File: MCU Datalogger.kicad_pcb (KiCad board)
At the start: 2 copper layers, 58.5 x 39.9 mm, 29 parts, among them J1 Conn_01x04_Pin, J2 Conn_01x04_Pin, J3 Conn_01x09_Pin, J4 Conn_02x03_Odd_Even, U1 24LC1025, U2 24LC1025, U3 DS1337S_, U4 ATMEGA328P-AU, Y1 32.768KHz, Y2 16MHz

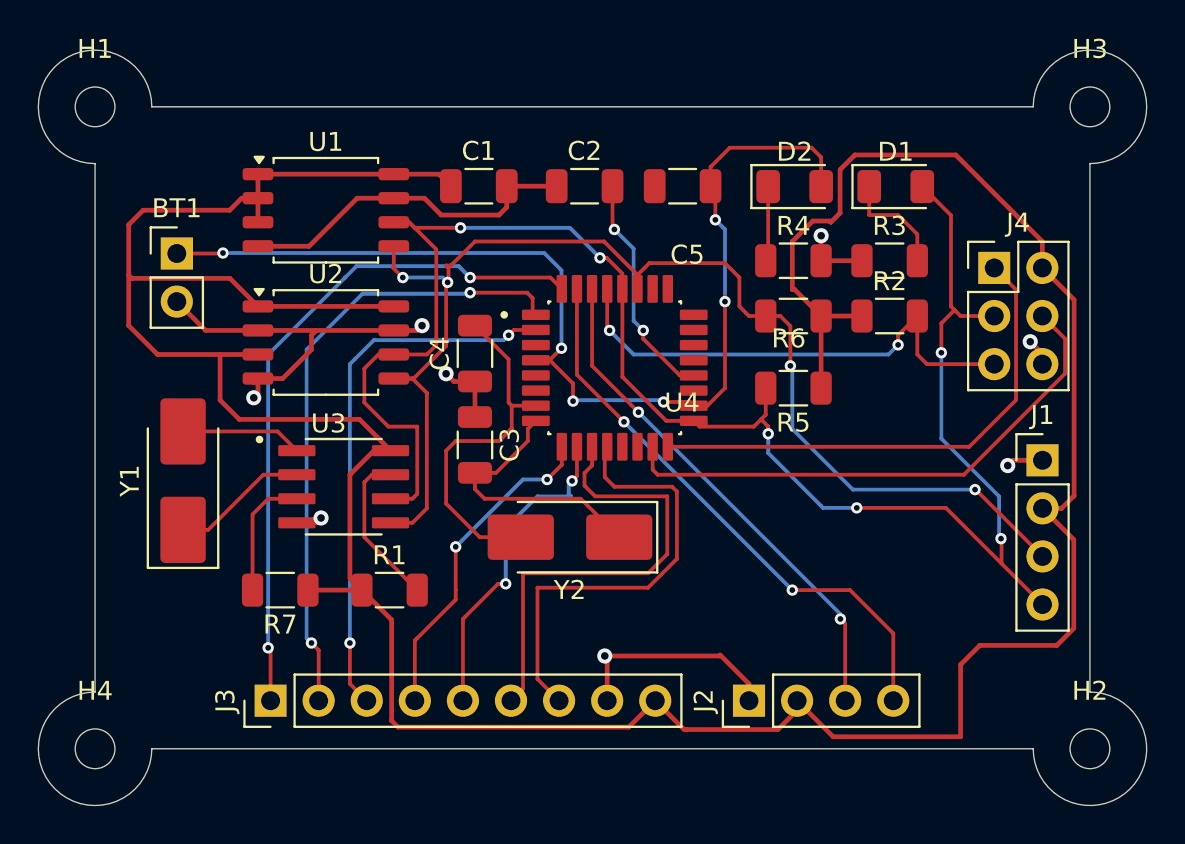
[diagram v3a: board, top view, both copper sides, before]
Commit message: routing done including copper fill
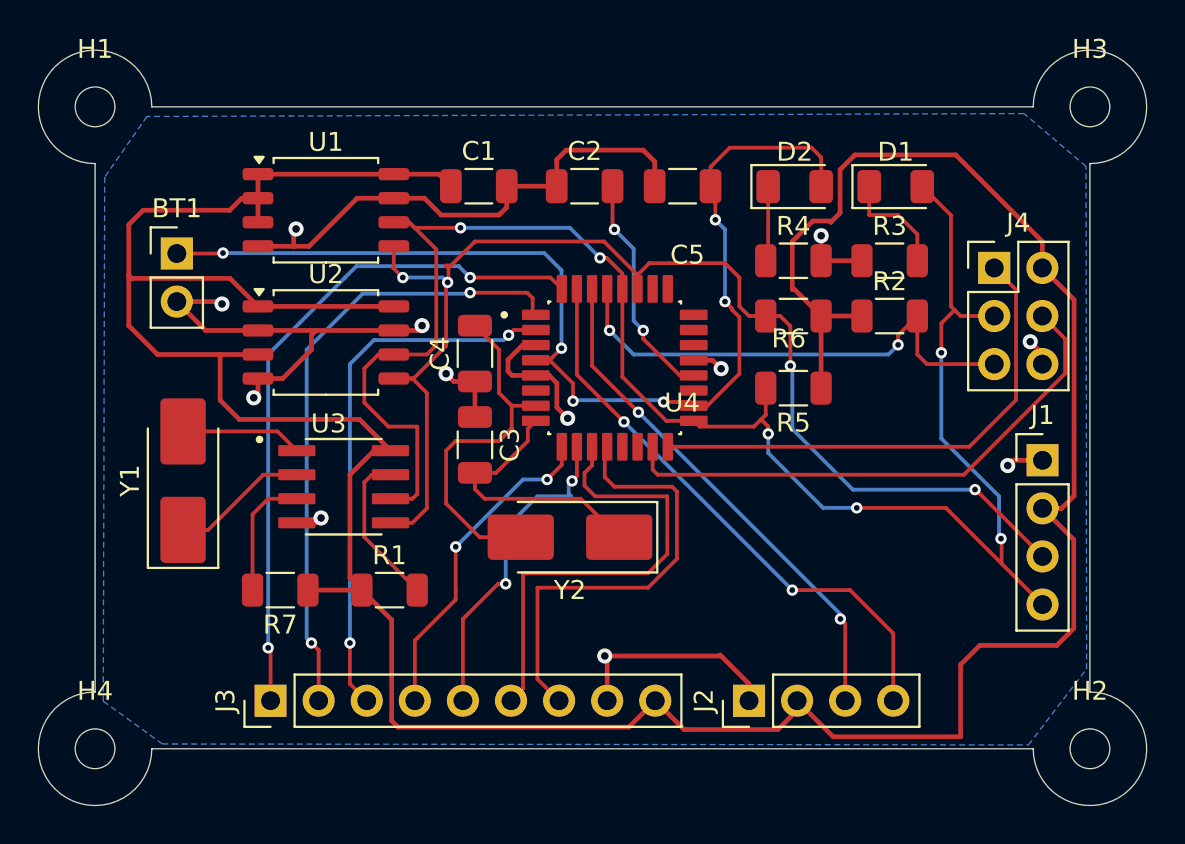
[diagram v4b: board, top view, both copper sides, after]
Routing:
- net GND: track 61.6 -> 82.3 mm, vias 8 -> 12
- added copper zone on B.Cu, net GND
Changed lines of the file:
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@@
+	)
+	(segment
+		(start 160.381 86.9071)
+		(end 160.381 86.848)
+		(width 0.2)
+		(layer "F.Cu")
+		(net 1)
+	)
+	(segment
+		(start 158.369 91.986)
+		(end 159.093 91.986)
+		(width 0.2)
+		(layer "F.Cu")
+		(net 1)
 	)
 	(segment
@@
 	)
 	(segment
-		(start 160.02 91.059)
-		(end 160.02 86.233)
+		(start 160.782 87.3081)
+		(end 160.381 86.9071)
+		(width 0.2)
+		(layer "F.Cu")
+		(net 1)
+	)
+	(segment
+		(start 159.093 91.986)
+		(end 160.782 90.297)
 		(width 0.2)
 		(layer "F.Cu")
@@
 	)
 	(segment
-		(start 159.093 91.986)
-		(end 160.02 91.059)
-		(width 0.2)
-		(layer "F.Cu")
-		(net 1)
-	)
-	(segment
 		(start 156.773965 91.790435)
 		(end 158.173435 91.790435)
@@
 	)
 	(segment
-		(start 160.02 86.233)
+		(start 160.381 86.848)
 		(end 160.02 86.487)
 		(width 0.2)
@@
 	)
 	(segment
+		(start 160.782 90.297)
+		(end 160.782 87.3081)
+		(width 0.2)
+		(layer "F.Cu")
+		(net 1)
+	)
+	(segment
 		(start 151.9936 90.8156)
 		(end 151.9936 91.7448)
@@
 	)
 	(segment
-		(start 158.369 91.986)
-		(end 159.093 91.986)
-		(width 0.2)
-		(layer "F.Cu")
-		(net 1)
-	)
-	(segment
 		(start 133.5024 83.9216)
 		(end 133.477 83.947)
@@
 	)
 	(segment
+		(start 151.13 80.391)
+		(end 151.13 78.994)
+		(width 0.25)
+		(layer "F.Cu")
+		(net 2)
+	)
+	(segment
+		(start 150.029 88.786)
+		(end 149.325622 88.786)
+		(width 0.25)
+		(layer "F.Cu")
+		(net 2)
+	)
+	(segment
+		(start 151.14 92.08132)
+		(end 151.710238 92.651558)
+		(width 0.25)
+		(layer "F.Cu")
+		(net 2)
+	)
+	(segment
+		(start 131.064 86.487)
+		(end 133.3246 86.487)
+		(width 0.25)
+		(layer "F.Cu")
+		(net 2)
+	)
+	(segment
 		(start 153.797 107.569)
 		(end 153.797 105.3338)
@@
 	)
 	(segment
+		(start 133.3246 86.487)
+		(end 133.4516 86.614)
+		(width 0.25)
+		(layer "F.Cu")
+		(net 2)
+	)
+	(segment
+		(start 151.13 78.994)
+		(end 151.638 78.486)
+		(width 0.25)
+		(layer "F.Cu")
+		(net 2)
+	)
+	(segment
 		(start 135.3505 91.3445)
 		(end 135.128 91.567)
@@
 	)
 	(segment
+		(start 150.029 90.386)
+		(end 150.732378 90.386)
+		(width 0.25)
+		(layer "F.Cu")
+		(net 2)
+	)
+	(segment
 		(start 159.7152 105.2068)
 		(end 159.766 105.156)
@@
 	)
 	(segment
+		(start 155.702 78.486)
+		(end 156.308 79.092)
+		(width 0.25)
+		(layer "F.Cu")
+		(net 2)
+	)
+	(segment
 		(start 132.588 88.011)
 		(end 135.3505 88.011)
@@
 	)
 	(segment
+		(start 159.3718 89.586)
+		(end 159.8168 90.031)
+		(width 0.25)
+		(layer "F.Cu")
+		(net 2)
+	)
+	(segment
+		(start 151.638 78.486)
+		(end 155.702 78.486)
+		(width 0.25)
+		(layer "F.Cu")
+		(net 2)
+	)
+	(segment
 		(start 136.652 90.551)
 		(end 138.176 89.027)
@@
 	)
 	(segment
+		(start 148.774 90.386)
+		(end 150.029 90.386)
+		(width 0.25)
+		(layer "F.Cu")
+		(net 2)
+	)
+	(segment
 		(start 143.764 88.011)
 		(end 144.018 87.757)
@@
 	)
 	(segment
+		(start 137.2362 82.7786)
+		(end 137.3632 82.6516)
+		(width 0.25)
+		(layer "F.Cu")
+		(net 2)
+	)
+	(segment
 		(start 159.766 105.156)
 		(end 161.29 106.68)
@@
 	)
 	(segment
+		(start 156.308 79.092)
+		(end 156.308 80.391)
+		(width 0.25)
+		(layer "F.Cu")
+		(net 2)
+	)
+	(segment
+		(start 137.2362 83.566)
+		(end 137.2362 82.7786)
+		(width 0.25)
+		(layer "F.Cu")
+		(net 2)
+	)
+	(segment
+		(start 135.3505 83.566)
+		(end 137.2362 83.566)
+		(width 0.25)
+		(layer "F.Cu")
+		(net 2)
+	)
+	(segment
 		(start 140.589 81.026)
 		(end 142.5255 81.026)
@@
 	)
 	(segment
+		(start 148.558 89.553622)
+		(end 148.558 90.17)
+		(width 0.25)
+		(layer "F.Cu")
+		(net 2)
+	)
+	(segment
 		(start 138.049 83.566)
 		(end 140.589 81.026)
@@
 	)
 	(segment
-		(start 135.3505 83.566)
+		(start 137.2362 83.566)
 		(end 138.049 83.566)
+		(width 0.25)
+		(layer "F.Cu")
+		(net 2)
+	)
+	(segment
+		(start 151.14 90.793622)
+		(end 151.14 92.08132)
 		(width 0.25)
 		(layer "F.Cu")
@@
 	)
 	(segment
+		(start 150.732378 90.386)
+		(end 151.14 90.793622)
+		(width 0.25)
+		(layer "F.Cu")
+		(net 2)
+	)
+	(segment
 		(start 135.3505 90.551)
 		(end 136.652 90.551)
@@
 	)
 	(segment
+		(start 149.325622 88.786)
+		(end 148.558 89.553622)
+		(width 0.25)
+		(layer "F.Cu")
+		(net 2)
+	)
+	(segment
 		(start 145.034 81.915)
 		(end 148.082 81.915)
@@
 	)
 	(segment
+		(start 148.558 90.17)
+		(end 148.774 90.386)
+		(width 0.25)
+		(layer "F.Cu")
+		(net 2)
+	)
+	(segment
 		(start 146.812 92.583)
 		(end 146.812 90.707)
@@
 		(start 165.098 83.0092)
 		(end 165.1 83.0072)
+		(width 0.25)
+		(layer "F.Cu")
+		(net 2)
+	)
+	(segment
+		(start 158.369 89.586)
+		(end 159.3718 89.586)
 		(width 0.25)
 		(layer "F.Cu")
@@
 	)
 	(via
+		(at 159.8168 90.031)
+		(size 0.8)
+		(drill 0.4)
+		(layers "F.Cu" "B.Cu")
+		(net 2)
+	)
+	(via
 		(at 165.1 83.0072)
 		(size 0.8)
@@
 	)
 	(via
+		(at 137.3632 82.6516)
+		(size 0.8)
+		(drill 0.4)
+		(layers "F.Cu" "B.Cu")
+		(net 2)
+	)
+	(via
+		(at 133.4516 86.614)
+		(size 0.8)
+		(drill 0.4)
+		(layers "F.Cu" "B.Cu")
+		(net 2)
+	)
+	(via
 		(at 135.128 91.567)
 		(size 0.8)
@@
 	)
 	(via
+		(at 151.710238 92.651558)
+		(size 0.8)
+		(drill 0.4)
+		(layers "F.Cu" "B.Cu")
+		(net 2)
+	)
+	(via
 		(at 145.288 90.297)
 		(size 0.8)
@@
 	)
 	(segment
+		(start 148.082 91.313)
+		(end 148.755 91.986)
+		(width 0.2)
+		(layer "F.Cu")
+		(net 6)
+	)
+	(segment
+		(start 148.082 89.027)
+		(end 148.082 91.313)
+		(width 0.2)
+		(layer "F.Cu")
+		(net 6)
+	)
+	(segment
 		(start 147.066 98.933)
 		(end 145.288 97.155)
@@
 	)
 	(segment
-		(start 146.812 87.757)
-		(end 148.59 89.535)
-		(width 0.2)
-		(layer "F.Cu")
-		(net 6)
-	)
-	(segment
 		(start 145.796 93.853)
 		(end 148.082 93.853)
@@
 	)
 	(segment
-		(start 148.59 89.535)
-		(end 148.59 91.821)
-		(width 0.2)
-		(layer "F.Cu")
-		(net 6)
-	)
-	(segment
-		(start 148.59 91.821)
-		(end 148.755 91.986)
+		(start 146.812 87.757)
+		(end 148.082 89.027)
 		(width 0.2)
 		(layer "F.Cu")
@@
 		(net 26)
 	)
+	(zone
+		(net 2)
+		(net_name "GND")
+		(layer "B.Cu")
+		(hatch edge 0.5)
+		(connect_pads
+			(clearance 0.5)
+		)
+		(min_thickness 0.25)
+		(filled_areas_thickness no)
+		(fill yes
+			(mode hatch)
+			(thermal_gap 0.5)
+			(thermal_bridge_width 0.5)
+			(hatch_thickness 1)
+			(hatch_gap 1.5)
+			(hatch_orientation 0)
+			(hatch_border_algorithm hatch_thickness)
+			(hatch_min_hole_area 0.3)
+		)
+		(polygon
+			(pts
+				(xy 175.8188 76.5556) (xy 129.4892 76.708) (xy 127.254 79.9084) (xy 127.1778 107.5944) (xy 130.302 109.855)
+				(xy 176.0474 109.9058) (xy 179.1208 105.8926) (xy 179.0954 79.3496)
+			)
+		)
+	)
 	(embedded_fonts no)

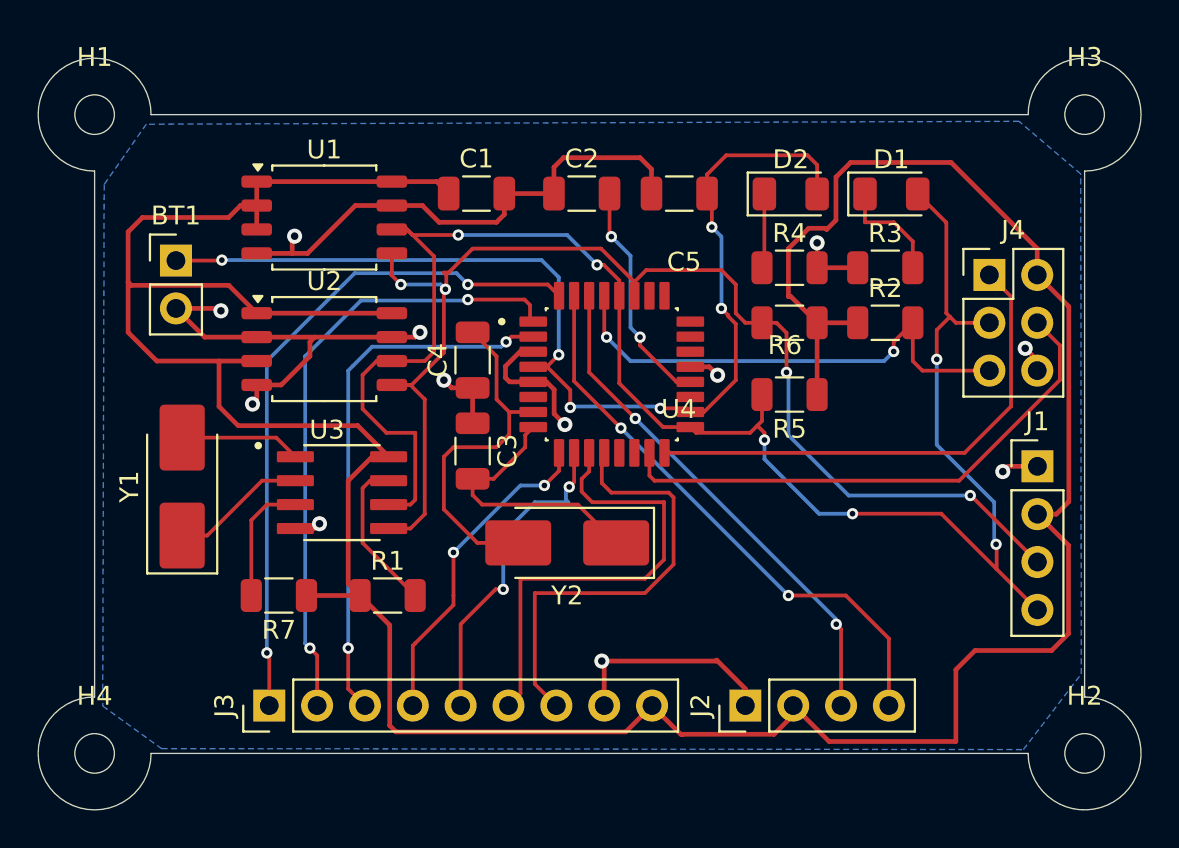
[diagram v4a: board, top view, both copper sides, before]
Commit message: silk screen labelling + routing + drc done
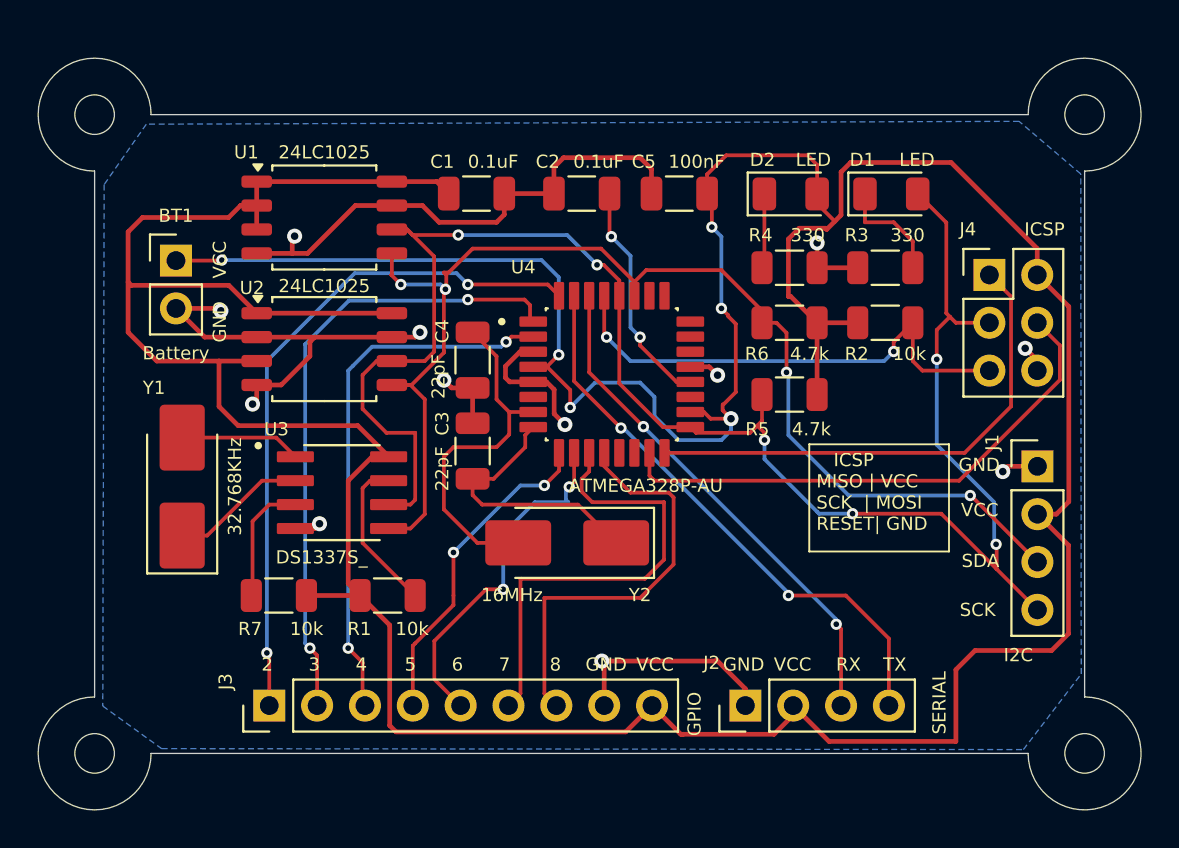
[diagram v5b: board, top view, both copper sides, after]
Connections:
- BT1 pad 1: Net-(BT1-+) -> /Vcc
- C5 pad 1: Net-(BT1-+) -> /Vcc
- D2 pad 2: Net-(BT1-+) -> /Vcc
- U4 pad 18: Net-(BT1-+) -> /Vcc
- U4 pad 4: Net-(BT1-+) -> /Vcc
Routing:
- net /Vcc: track 175.4 -> 243.5 mm, vias 0 -> 6
- net Net-(BT1-+): track 59.0 -> 0.00 mm, vias 6 -> 0
- net /D8: track 23.8 -> 22.3 mm
- net /D6: track 17.3 -> 18.7 mm
- net /SDA: track 66.8 -> 66.2 mm
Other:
- board text added: "2"
- board text added: "3"
- board text added: "4"
- board text added: "5"
- board text added: "6"
- board text added: "7"
- board text added: "8"
- board text added: "Data logger with ATMEGA328p-AU"
- board text added: "GND"
- board text added: "GPIO"
- board text added: "I2C"
- board text added: "ICSP"
- board text added: "ICSP MISO | VCC SCK | MOSI RESET| GND"
- board text added: "RX"
- board text added: "SCK"
- board text added: "SDA"
- board text added: "SERIAL"
- board text added: "TX"
- board text added: "Tunmise"
- board text added: "VCC"

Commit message: Saved gerbers + completed project ish
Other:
- board text added: "0.0000 mm / 0.0000 mm"
- board text added: "0.3000 mm"
- board text added: "1.6000 mm"
- board text added: "58.5511 mm x 39.9075 mm"
- board text added: "BOARD CHARACTERISTICS"
- board text added: "Board Thickness:"
- board text added: "Board overall dimensions:"
- board text added: "Castellated pads:"
- board text added: "Copper Finish:"
- board text added: "Copper Layer Count:"
- board text added: "Edge card connectors:"
- board text added: "Impedance Control:"
- board text added: "Min hole diameter:"
- board text added: "Min track/spacing:"
- board text added: "No"
- board text added: "None"
- board text added: "Plated Board Edge:"
